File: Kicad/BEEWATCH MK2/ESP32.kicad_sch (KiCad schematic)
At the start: 42 parts, among them J1 USB_C_Receptacle_USB2.0_16P, Q1 DMG6968U, SW1 TK-074-4, SW2 TK-074-4, U1 ESP32-S3FH4R2, Y1 40MHz, Y2 32.768KHz

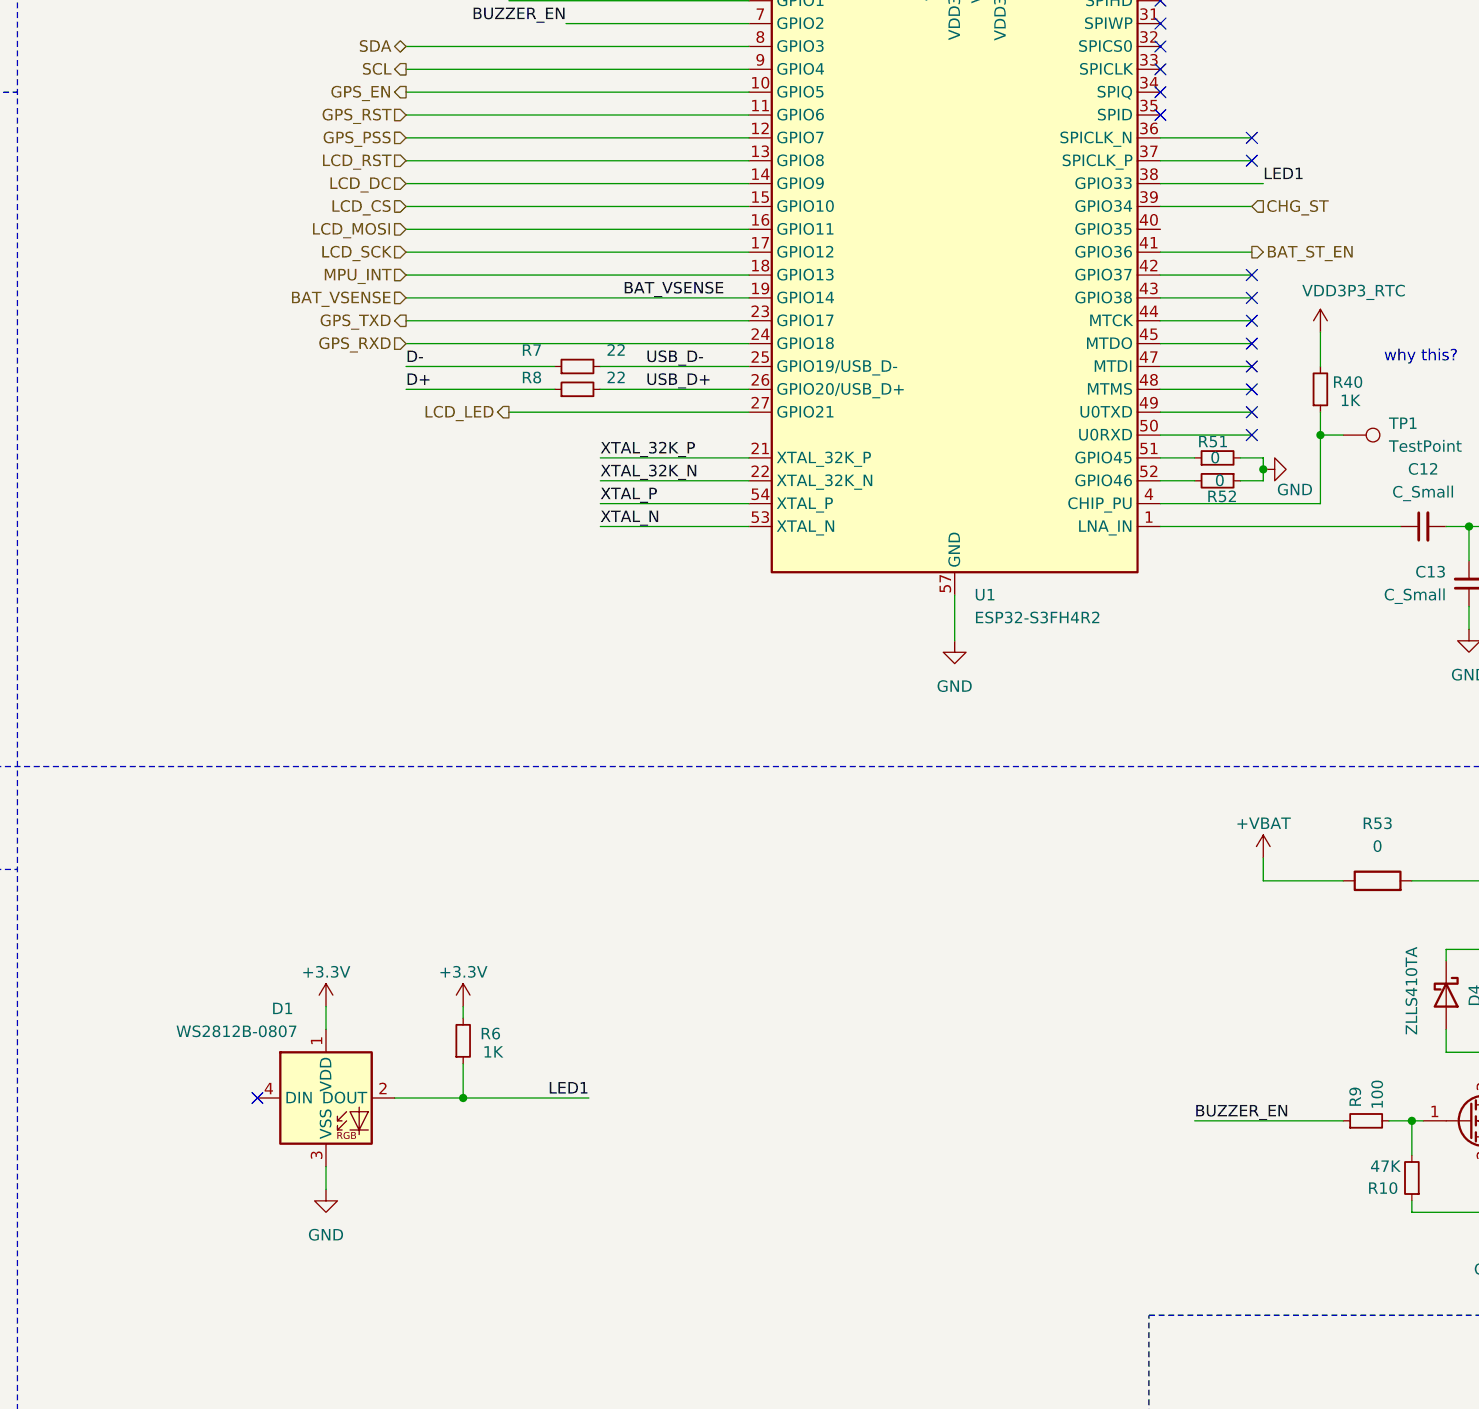
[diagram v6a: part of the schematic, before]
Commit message: Added display board schema
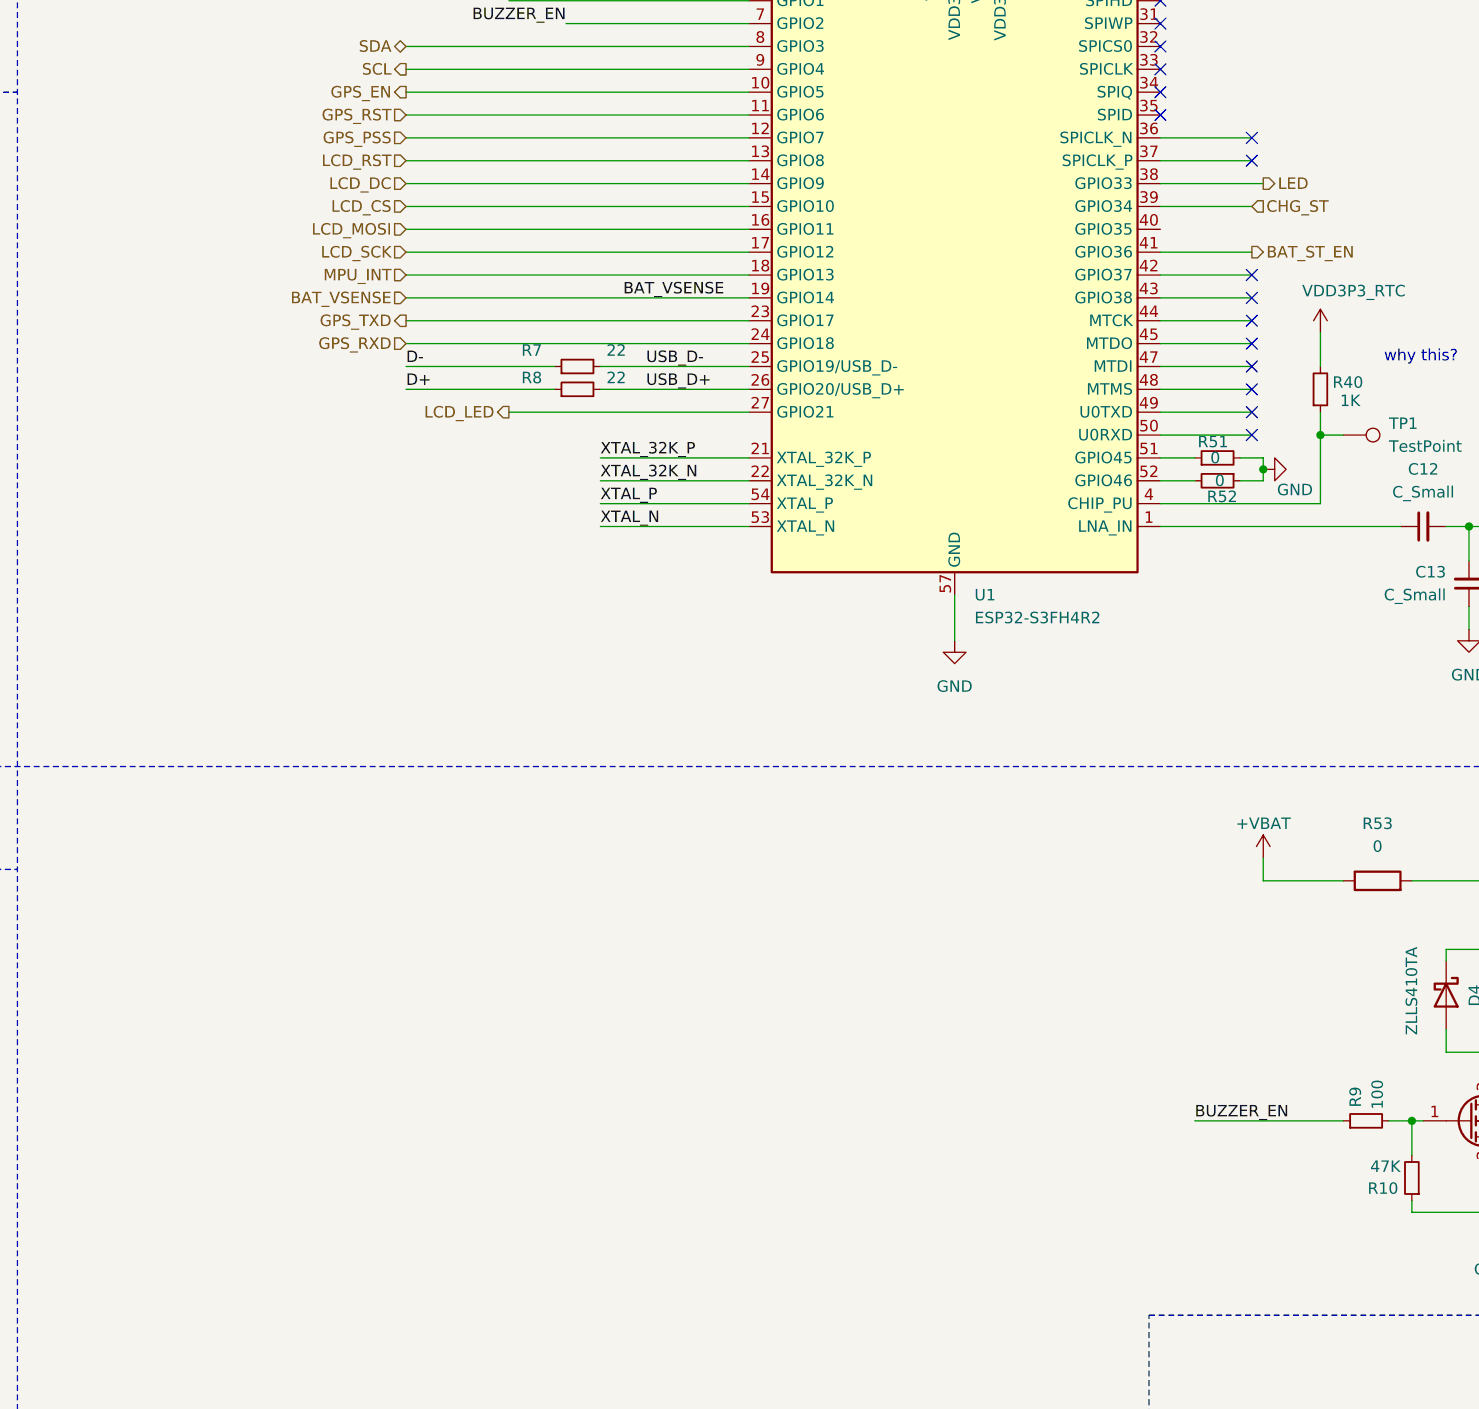
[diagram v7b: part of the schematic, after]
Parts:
- removed D1: WS2812B-0807, SM_LED:XL-0807RGBC-WS2812B, symbol SM_LED:WS2812B-0807
- removed R6: 1K, Resistor_SMD:R_0402_1005Metric_Pad0.72x0.64mm_HandSolder, symbol Device:R_Small
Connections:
- net LED1 renamed LED
- no-connect marks 22 -> 21

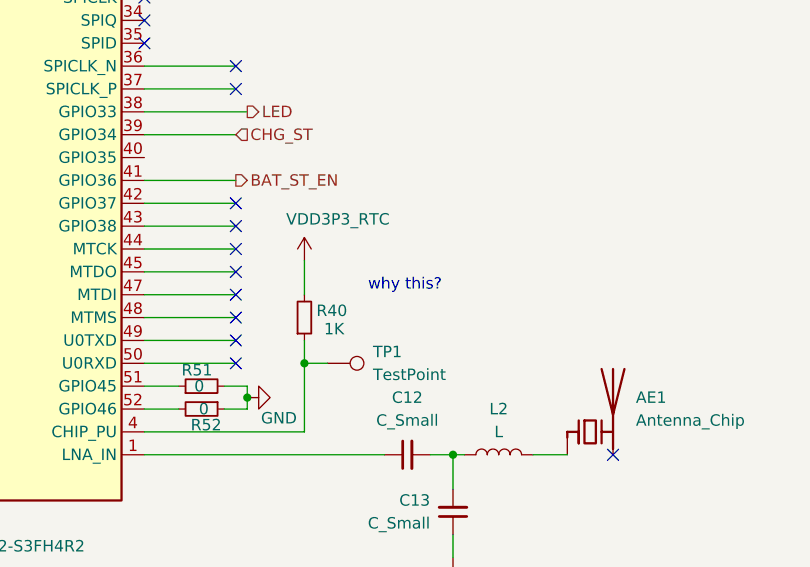
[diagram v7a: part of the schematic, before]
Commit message: Added SMA connector
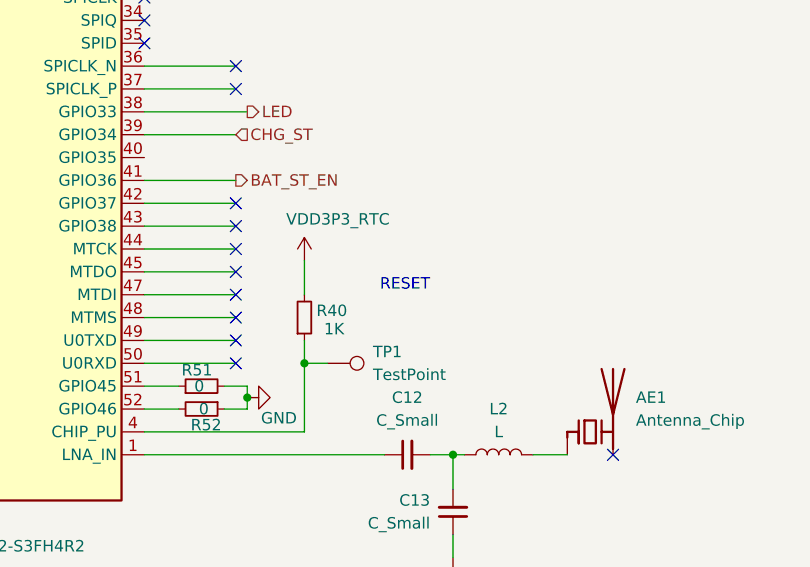
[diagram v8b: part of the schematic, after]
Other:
- note added: "RESET"
- note removed: "why this?"
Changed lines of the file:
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@@
 		)
 	)
-	(text "why this?\n"
+	(text "RESET\n"
 		(exclude_from_sim no)
 		(at 324.866 139.954 0)
